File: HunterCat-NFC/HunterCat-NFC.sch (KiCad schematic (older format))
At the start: 60 parts, among them P1 USB_C_Plug_USB2.0, SW1 RESET, U1 ATSAMD21E18A, U2 PN7150B0HN/C11004, U3 MCP73831-3-OT, Y1 27.12Mhz

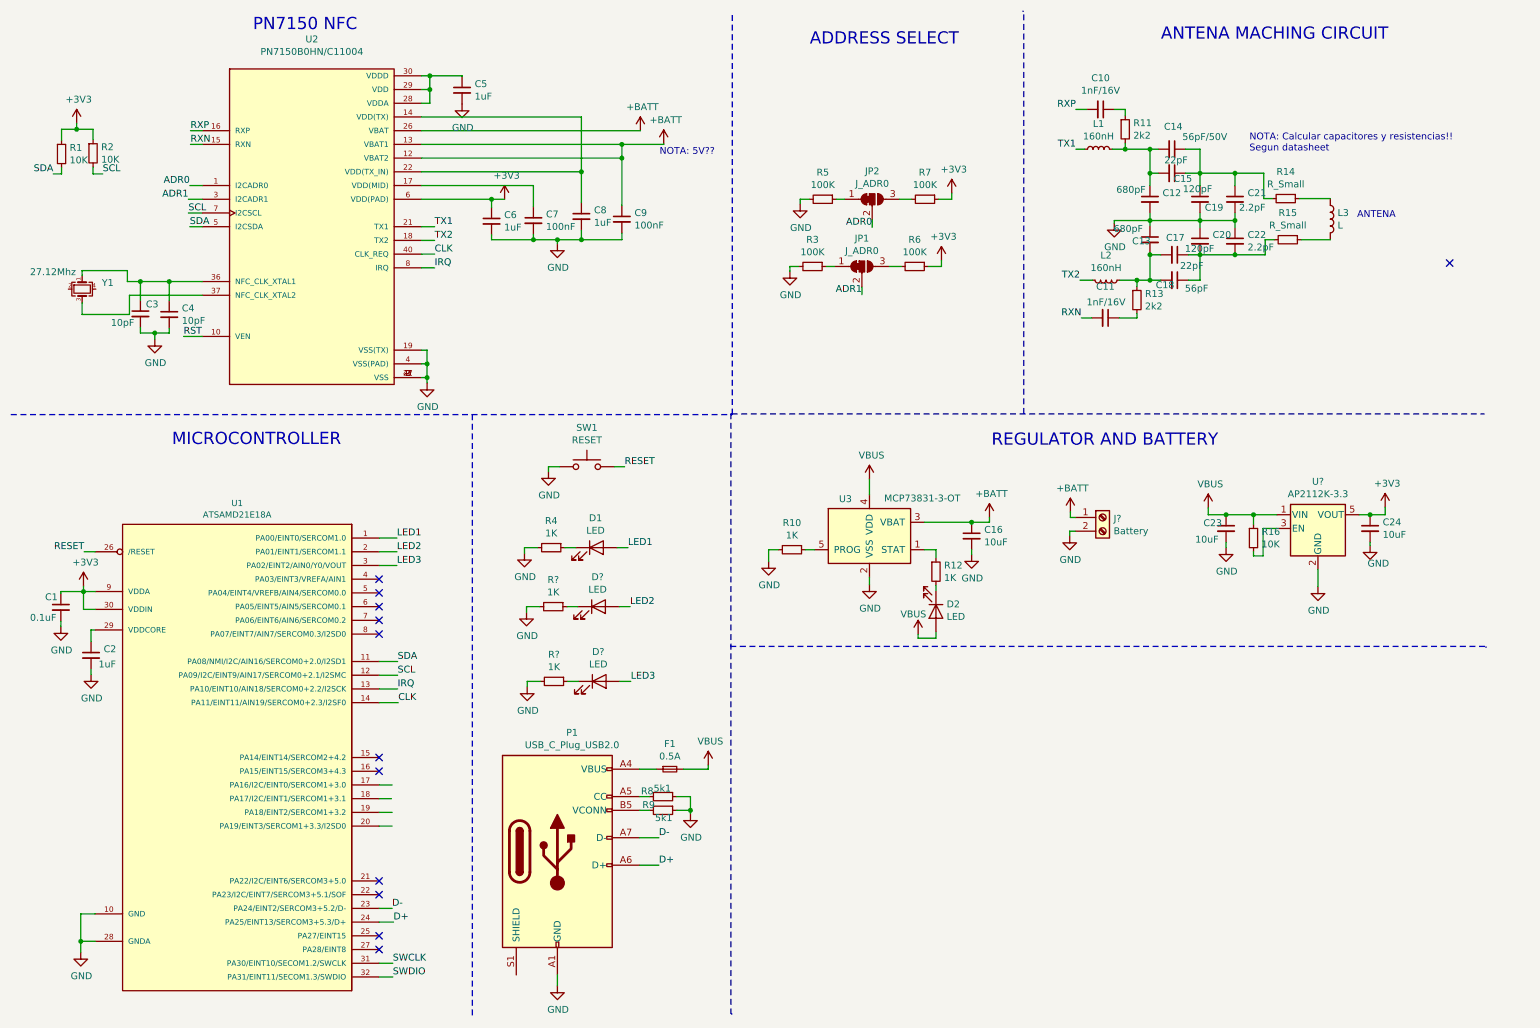
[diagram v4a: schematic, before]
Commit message: add SPI flash and ADC Battery
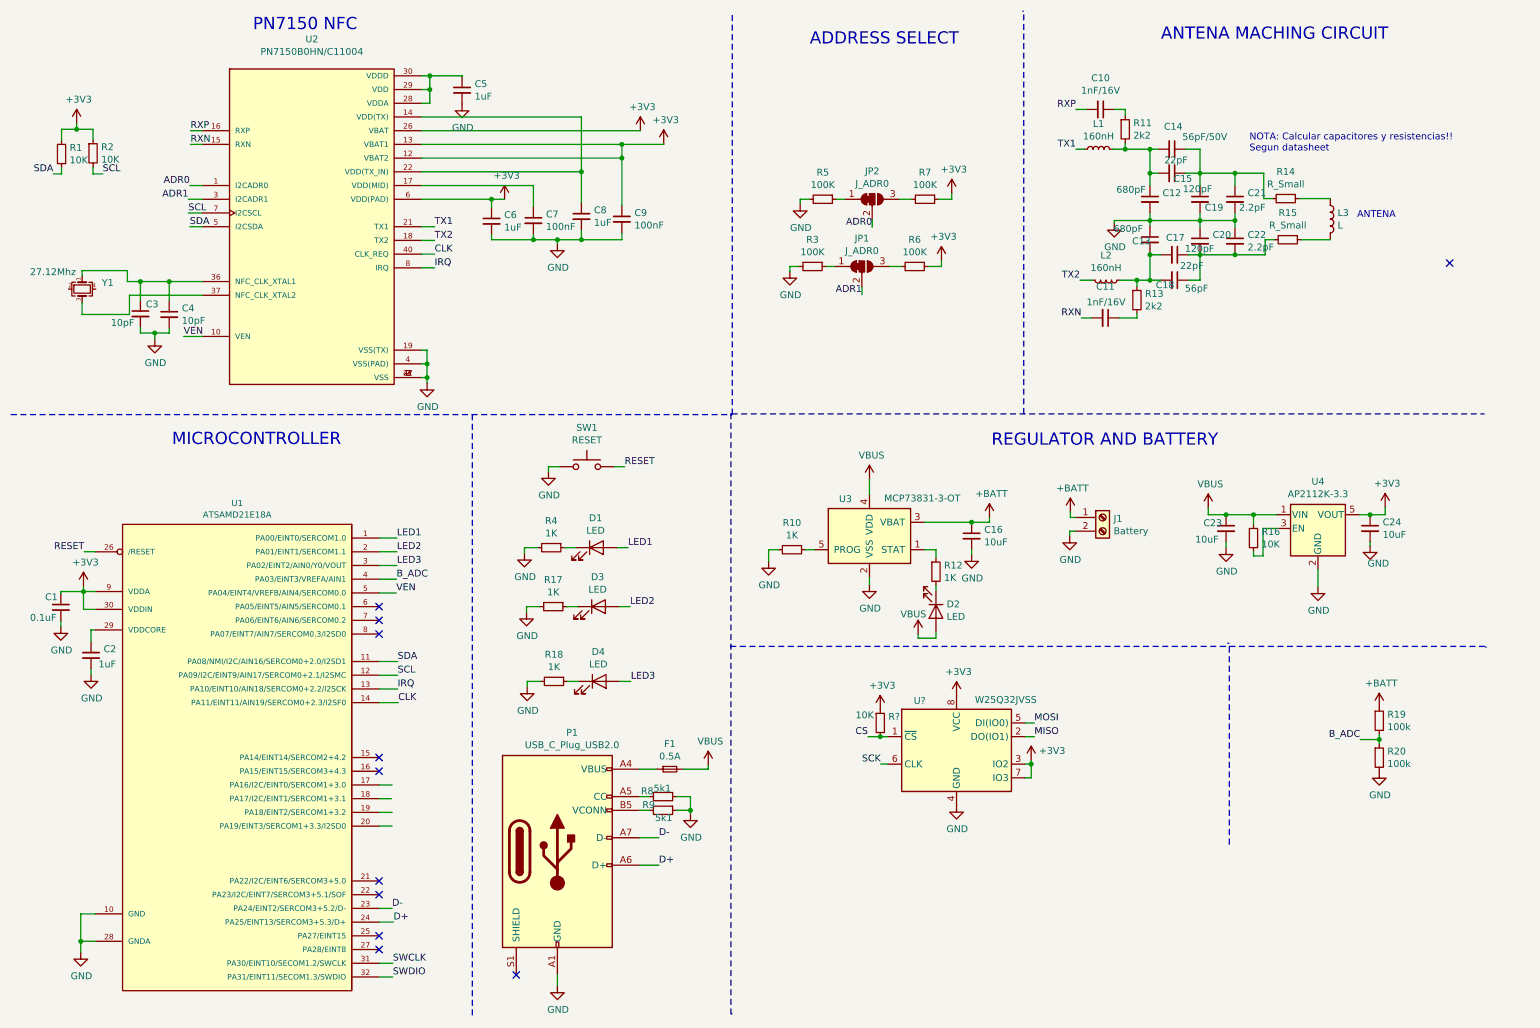
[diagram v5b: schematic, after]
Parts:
- added R19, R20: 100k, symbol Device:R_Small
- added R?: 10K, symbol Device:R_Small
- added U?: W25Q32JVSS, Package_SO:SOIC-8_5.23x5.23mm_P1.27mm, symbol Memory_Flash:W25Q32JVSS
- gave numbers to parts that had none: 6
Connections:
- net RST is gone; now on net VEN: U2.10 (VEN)
- net +3V3: now also C9.1, U2.12 (VBAT2), U2.13 (VBAT1), U2.26 (VBAT), R?.1, U?.3 (IO2), U?.7 (IO3), U?.8 (VCC)
- net +BATT: now also R19.1; no longer C9.1, U2.12 (VBAT2), U2.13 (VBAT1), U2.26 (VBAT)
- net GND: now also R20.2, U?.4 (GND)
- net B_ADC: now reaches U1.4 (PA03/EINT3/VREFA/AIN1)
- net B_ADC: now also R19.2, R20.1
- net VEN: now reaches U1.5 (PA04/EINT4/VREFB/AIN4/SERCOM0.0)
- new net CS: R?.2, U?.1 (~CS)
- new net MISO: U?.2 (DO(IO1))
- new net MOSI: U?.5 (DI(IO0))
- new net SCK: U?.6 (CLK)
- no-connect marks 12 -> 11
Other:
- note removed: "NOTA: 5V??"
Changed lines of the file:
@@
 Connection ~ 4920 1440
-Wire Wire Line
-	3460 1340 5055 1340
 Wire Wire Line
 	3970 1840 4065 1840
@@
 	1860 2840 1725 2840
 Text Label 1725 2840 0    50   ~ 0
-RST
+VEN
 Wire Notes Line
 	465  3410 5725 3410
@@
 	1    0    0    -1
 $EndComp
-$Comp
-L power:+BATT #PWR016
-U 1 1 5E486C1E
-P 5055 1340
-F 0 "#PWR016" H 5055 1190 50  0001 C CNN
-F 1 "+BATT" H 5070 1513 50  0000 C CNN
-F 2 "" H 5055 1340 50  0001 C CNN
-F 3 "" H 5055 1340 50  0001 C CNN
-	1    5055 1340
-	1    0    0    -1
-$EndComp
-$Comp
-L power:+BATT #PWR017
-U 1 1 5E4874CB
-P 5225 1435
-F 0 "#PWR017" H 5225 1285 50  0001 C CNN
-F 1 "+BATT" H 5240 1608 50  0000 C CNN
-F 2 "" H 5225 1435 50  0001 C CNN
-F 3 "" H 5225 1435 50  0001 C CNN
-	1    5225 1435
-	1    0    0    -1
-$EndComp
 Wire Wire Line
 	5225 1440 5225 1435
 Wire Wire Line
 	4920 1440 5225 1440
-Text Notes 5195 1525 0    50   ~ 0
-NOTA: 5V??
 $Comp
 L Device:R_Small R1
@@
 $EndComp
 $Comp
-L Connector:Screw_Terminal_01x02 J?
+L Connector:Screw_Terminal_01x02 J1
 U 1 1 5E75338C
 P 8425 4160
-F 0 "J?" H 8505 4152 50  0000 L CNN
+F 0 "J1" H 8505 4152 50  0000 L CNN
 F 1 "Battery" H 8505 4061 50  0000 L CNN
 F 2 "" H 8425 4160 50  0001 C CNN
@@
 	8185 4260 8185 4295
 $Comp
-L power:GND #PWR?
+L power:GND #PWR0101
 U 1 1 5E76E2B6
 P 8185 4295
-F 0 "#PWR?" H 8185 4045 50  0001 C CNN
+F 0 "#PWR0101" H 8185 4045 50  0001 C CNN
 F 1 "GND" H 8190 4122 50  0000 C CNN
 F 2 "" H 8185 4295 50  0001 C CNN
@@
 $EndComp
 $Comp
-L power:+BATT #PWR?
+L power:+BATT #PWR0102
 U 1 1 5E76EF50
 P 8190 4120
-F 0 "#PWR?" H 8190 3970 50  0001 C CNN
+F 0 "#PWR0102" H 8190 3970 50  0001 C CNN
 F 1 "+BATT" H 8205 4293 50  0000 C CNN
 F 2 "" H 8190 4120 50  0001 C CNN
@@
 $EndComp
 $Comp
-L Device:LED D?
+L Device:LED D3
 U 1 1 5E770C69
 P 4750 4810
-F 0 "D?" H 4743 5026 50  0000 C CNN
+F 0 "D3" H 4743 5026 50  0000 C CNN
 F 1 "LED" H 4743 4935 50  0000 C CNN
 F 2 "" H 4750 4810 50  0001 C CNN
@@
 $EndComp
 $Comp
-L Device:R_Small R?
+L Device:R_Small R17
 U 1 1 5E770C6F
 P 4420 4810
-F 0 "R?" V 4224 4810 50  0000 C CNN
+F 0 "R17" V 4224 4810 50  0000 C CNN
 F 1 "1K" V 4315 4810 50  0000 C CNN
 F 2 "" H 4420 4810 50  0001 C CNN
@@
 	4900 4810 4980 4810
 $Comp
-L power:GND #PWR?
+L power:GND #PWR0103
 U 1 1 5E770C79
 P 4225 4850
-F 0 "#PWR?" H 4225 4600 50  0001 C CNN
+F 0 "#PWR0103" H 4225 4600 50  0001 C CNN
 F 1 "GND" H 4230 4677 50  0000 C CNN
 F 2 "" H 4225 4850 50  0001 C CNN
@@
 LED2
 $Comp
-L Device:LED D?
+L Device:LED D4
 U 1 1 5E793493
 P 4755 5355
-F 0 "D?" H 4748 5571 50  0000 C CNN
+F 0 "D4" H 4748 5571 50  0000 C CNN
 F 1 "LED" H 4748 5480 50  0000 C CNN
 F 2 "" H 4755 5355 50  0001 C CNN
@@
 $EndComp
 $Comp
-L Device:R_Small R?
+L Device:R_Small R18
 U 1 1 5E793499
 P 4425 5355
-F 0 "R?" V 4229 5355 50  0000 C CNN
+F 0 "R18" V 4229 5355 50  0000 C CNN
 F 1 "1K" V 4320 5355 50  0000 C CNN
 F 2 "" H 4425 5355 50  0001 C CNN
@@
 	4905 5355 4985 5355
 $Comp
-L power:GND #PWR?
+L power:GND #PWR0104
 U 1 1 5E7934A3
 P 4230 5395
-F 0 "#PWR?" H 4230 5145 50  0001 C CNN
+F 0 "#PWR0104" H 4230 5145 50  0001 C CNN
 F 1 "GND" H 4235 5222 50  0000 C CNN
 F 2 "" H 4230 5395 50  0001 C CNN
@@
 Text Label 4985 5355 0    50   ~ 0
 LED3
-NoConn ~ 3150 4610
-NoConn ~ 3150 4710
 NoConn ~ 3150 4810
 NoConn ~ 3150 4910
@@
 	7850 470  7840 470
 $Comp
-L Regulator_Linear:AP2112K-3.3 U?
+L Regulator_Linear:AP2112K-3.3 U4
 U 1 1 5E451F7B
 P 9995 4240
-F 0 "U?" H 9995 4582 50  0000 C CNN
+F 0 "U4" H 9995 4582 50  0000 C CNN
 F 1 "AP2112K-3.3" H 9995 4491 50  0000 C CNN
 F 2 "Package_TO_SOT_SMD:SOT-23-5" H 9995 4565 50  0001 C CNN
@@
 Wire Wire Line
 	9525 4440 9525 4410
+Wire Wire Line
+	3460 1340 5055 1340
+$Comp
+L power:+3V3 #PWR0105
+U 1 1 5E67D6C7
+P 5225 1435
+F 0 "#PWR0105" H 5225 1285 50  0001 C CNN
+F 1 "+3V3" H 5240 1608 50  0000 C CNN
+F 2 "" H 5225 1435 50  0001 C CNN
+F 3 "" H 5225 1435 50  0001 C CNN
+	1    5225 1435
+	1    0    0    -1
+$EndComp
+$Comp
+L power:+3V3 #PWR0106
+U 1 1 5E67E264
+P 5055 1340
+F 0 "#PWR0106" H 5055 1190 50  0001 C CNN
+F 1 "+3V3" H 5070 1513 50  0000 C CNN
+F 2 "" H 5055 1340 50  0001 C CNN
+F 3 "" H 5055 1340 50  0001 C CNN
+	1    5055 1340
+	1    0    0    -1
+$EndComp
+Wire Wire Line
+	3150 4710 3275 4710
+Text Label 3275 4710 0    50   ~ 0
+VEN
+Wire Wire Line
+	3150 4610 3277 4610
+Text Label 3277 4610 0    50   ~ 0
+B_ADC
+$Comp
+L Device:R_Small R19
+U 1 1 5E6BD0A2
+P 10442 5642
+F 0 "R19" H 10501 5688 50  0000 L CNN
+F 1 "100k" H 10501 5597 50  0000 L CNN
+F 2 "" H 10442 5642 50  0001 C CNN
+F 3 "~" H 10442 5642 50  0001 C CNN
+	1    10442 5642
+	1    0    0    -1
+$EndComp
+$Comp
+L Device:R_Small R20
+U 1 1 5E6BDB90
+P 10442 5911
+F 0 "R20" H 10501 5957 50  0000 L CNN
+F 1 "100k" H 10501 5866 50  0000 L CNN
+F 2 "" H 10442 5911 50  0001 C CNN
+F 3 "~" H 10442 5911 50  0001 C CNN
+	1    10442 5911
+	1    0    0    -1
+$EndComp
+Wire Wire Line
+	10442 5742 10442 5779
+Wire Wire Line
+	10442 5779 10303 5779
+Connection ~ 10442 5779
+Wire Wire Line
+	10442 5779 10442 5811
+Text Label 10303 5779 2    50   ~ 0
+B_ADC
+$Comp
+L power:+BATT #PWR0107
+U 1 1 5E6DD27D
+P 10442 5542
+F 0 "#PWR0107" H 10442 5392 50  0001 C CNN
+F 1 "+BATT" H 10457 5715 50  0000 C CNN
+F 2 "" H 10442 5542 50  0001 C CNN
+F 3 "" H 10442 5542 50  0001 C CNN
+	1    10442 5542
+	1    0    0    -1
+$EndComp
+$Comp
+L power:GND #PWR0108
+U 1 1 5E6DE2AB
+P 10442 6011
+F 0 "#PWR0108" H 10442 5761 50  0001 C CNN
+F 1 "GND" H 10447 5838 50  0000 C CNN
+F 2 "" H 10442 6011 50  0001 C CNN
+F 3 "" H 10442 6011 50  0001 C CNN
+	1    10442 6011
+	1    0    0    -1
+$EndComp
+NoConn ~ 4150 7495
+Wire Notes Line
+	9349 6545 9349 5077
+Wire Notes Line
+	9349 5077 9335 5077
+$Comp
+L Memory_Flash:W25Q32JVSS U?
+U 1 1 5E73BDBA
+P 7360 5858
+F 0 "U?" H 7091 6220 50  0000 C CNN
+F 1 "W25Q32JVSS" H 7719 6227 50  0000 C CNN
+F 2 "Package_SO:SOIC-8_5.23x5.23mm_P1.27mm" H 7360 5858 50  0001 C CNN
+F 3 "http://www.winbond.com/resource-files/w25q32jv%20revg%2003272018%20plus.pdf" H 7360 5858 50  0001 C CNN
+	1    7360 5858
+	1    0    0    -1
+$EndComp
+$Comp
+L power:GND #PWR?
+U 1 1 5E73D4E9
+P 7360 6258
+F 0 "#PWR?" H 7360 6008 50  0001 C CNN
+F 1 "GND" H 7365 6085 50  0000 C CNN
+F 2 "" H 7360 6258 50  0001 C CNN
+F 3 "" H 7360 6258 50  0001 C CNN
+	1    7360 6258
+	1    0    0    -1
+$EndComp
+$Comp
+L power:+3V3 #PWR?
+U 1 1 5E73E614
+P 7360 5458
+F 0 "#PWR?" H 7360 5308 50  0001 C CNN
+F 1 "+3V3" H 7375 5631 50  0000 C CNN
+F 2 "" H 7360 5458 50  0001 C CNN
+F 3 "" H 7360 5458 50  0001 C CNN
+	1    7360 5458
+	1    0    0    -1
+$EndComp
+Wire Wire Line
+	7905 6058 7905 5958
+Wire Wire Line
+	7905 5958 7904 5958
+Wire Wire Line
+	7860 6058 7905 6058
+Wire Wire Line
+	7904 5958 7904 5928
+Connection ~ 7904 5958
+Wire Wire Line
+	7904 5958 7860 5958
+$Comp
+L power:+3V3 #PWR?
+U 1 1 5E76F067
+P 7904 5928
+F 0 "#PWR?" H 7904 5778 50  0001 C CNN
+F 1 "+3V3" H 8057 5995 50  0000 C CNN
+F 2 "" H 7904 5928 50  0001 C CNN
+F 3 "" H 7904 5928 50  0001 C CNN
+	1    7904 5928
+	1    0    0    -1
+$EndComp
+Wire Wire Line
+	7860 5658 7927 5658
+Wire Wire Line
+	7860 5758 7928 5758
+Wire Wire Line
+	6860 5758 6804 5758
+Wire Wire Line
+	6860 5958 6807 5958
+$Comp
+L Device:R_Small R?
+U 1 1 5E7C0D45
+P 6804 5658
+F 0 "R?" H 6863 5704 50  0000 L CNN
+F 1 "10K" H 6624 5715 50  0000 L CNN
+F 2 "" H 6804 5658 50  0001 C CNN
+F 3 "~" H 6804 5658 50  0001 C CNN
+	1    6804 5658
+	1    0    0    -1
+$EndComp
+$Comp
+L power:+3V3 #PWR?
+U 1 1 5E7C254D
+P 6804 5558
+F 0 "#PWR?" H 6804 5408 50  0001 C CNN
+F 1 "+3V3" H 6819 5731 50  0000 C CNN
+F 2 "" H 6804 5558 50  0001 C CNN
+F 3 "" H 6804 5558 50  0001 C CNN
+	1    6804 5558
+	1    0    0    -1
+$EndComp
+Text Label 6714 5758 2    50   ~ 0
+CS
+Wire Wire Line
+	6804 5758 6714 5758
+Connection ~ 6804 5758
+Text Label 6807 5958 2    50   ~ 0
+SCK
+Text Label 7928 5758 0    50   ~ 0
+MISO
+Text Label 7927 5658 0    50   ~ 0
+MOSI
 $EndSCHEMATC

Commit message: add SPI pins
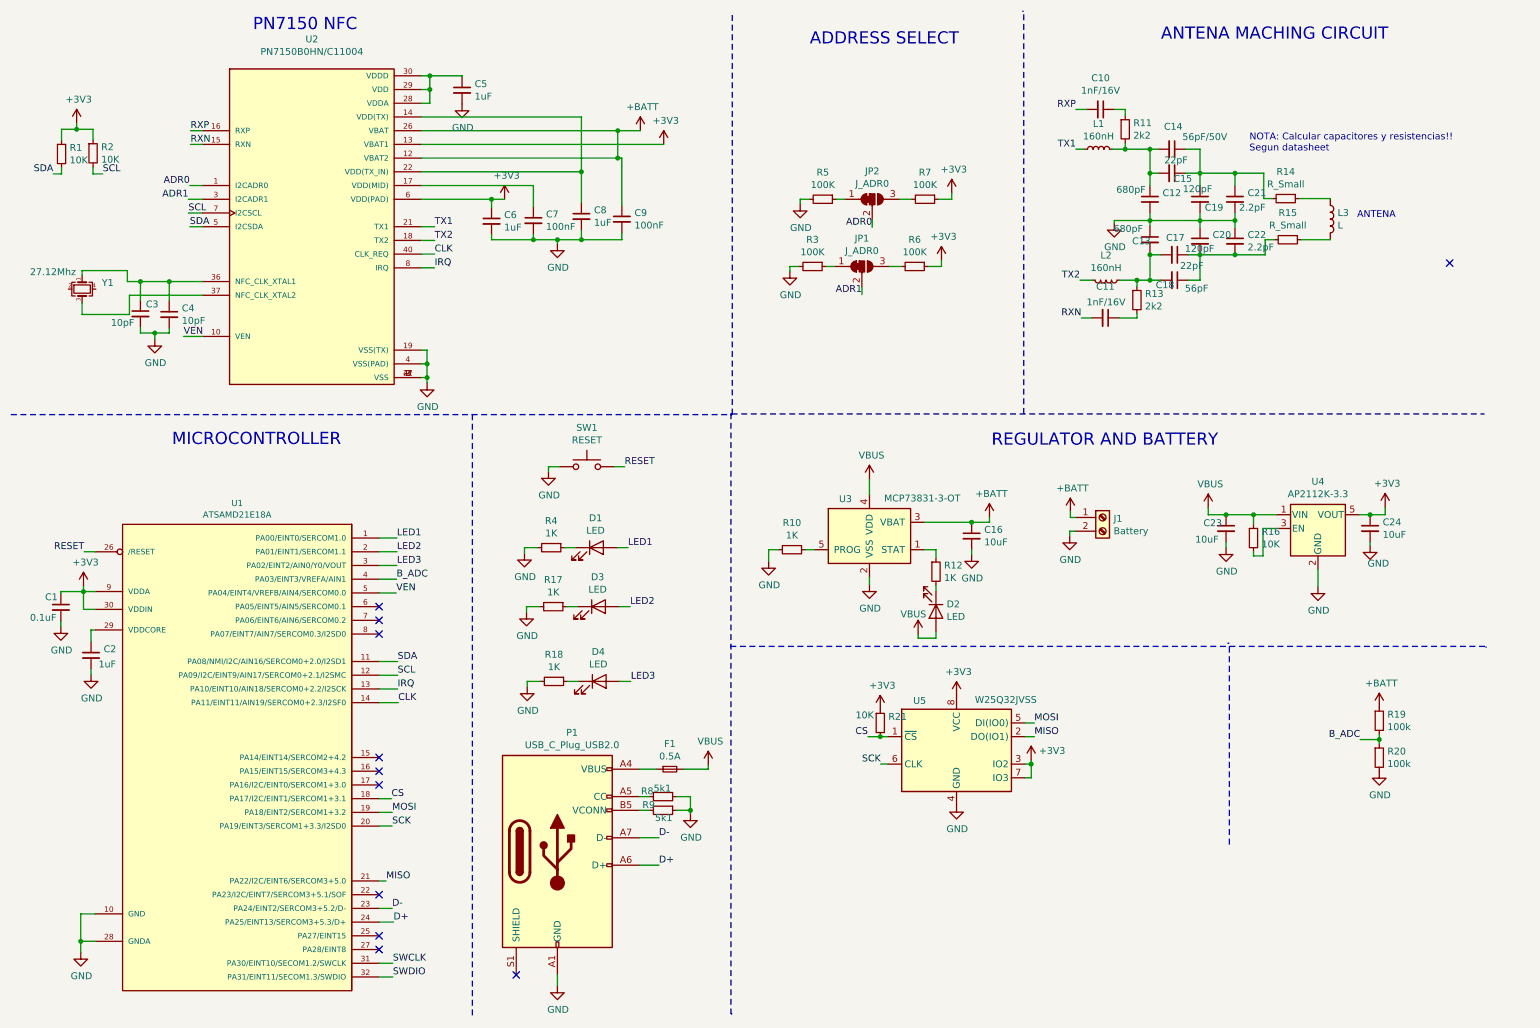
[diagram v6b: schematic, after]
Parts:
- gave numbers to parts that had none: 2
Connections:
- net +3V3: no longer C9.1, U2.12 (VBAT2), U2.26 (VBAT)
- net +BATT: now also C9.1, U2.12 (VBAT2), U2.26 (VBAT)
- net CS: now also U1.18 (PA17/I2C/EINT1/SERCOM1+3.1)
- net MISO: now also U1.21 (PA22/I2C/EINT6/SERCOM3+5.0)
- net MOSI: now also U1.19 (PA18/EINT2/SERCOM1+3.2)
- net SCK: now also U1.20 (PA19/EINT3/SERCOM1+3.3/I2SD0)
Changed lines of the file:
@@
 $EndComp
-Wire Wire Line
-	4920 1440 4920 1540
-Wire Wire Line
-	3460 1540 4920 1540
-Connection ~ 4920 1540
 Wire Wire Line
 	4920 1540 4920 1885
@@
 	1    0    0    -1
 $EndComp
-Wire Wire Line
-	3460 1440 4920 1440
-Connection ~ 4920 1440
 Wire Wire Line
 	3970 1840 4065 1840
@@
 	3150 6210 3240 6210
 Wire Wire Line
-	3150 6110 3245 6110
-Wire Wire Line
 	3150 6410 3245 6410
 Wire Wire Line
@@
 	1    0    0    -1
 $EndComp
-Wire Wire Line
-	5225 1440 5225 1435
-Wire Wire Line
-	4920 1440 5225 1440
 $Comp
 L Device:R_Small R1
@@
 NoConn ~ 3150 7210
 NoConn ~ 3150 6910
-NoConn ~ 3150 6810
 NoConn ~ 10955 2305
 Text Notes 7615 3650 0    89   ~ 0
@@
 	9525 4440 9525 4410
 Wire Wire Line
-	3460 1340 5055 1340
-$Comp
-L power:+3V3 #PWR0105
-U 1 1 5E67D6C7
-P 5225 1435
-F 0 "#PWR0105" H 5225 1285 50  0001 C CNN
-F 1 "+3V3" H 5240 1608 50  0000 C CNN
-F 2 "" H 5225 1435 50  0001 C CNN
-F 3 "" H 5225 1435 50  0001 C CNN
-	1    5225 1435
-	1    0    0    -1
-$EndComp
-$Comp
-L power:+3V3 #PWR0106
-U 1 1 5E67E264
-P 5055 1340
-F 0 "#PWR0106" H 5055 1190 50  0001 C CNN
-F 1 "+3V3" H 5070 1513 50  0000 C CNN
-F 2 "" H 5055 1340 50  0001 C CNN
-F 3 "" H 5055 1340 50  0001 C CNN
-	1    5055 1340
-	1    0    0    -1
-$EndComp
+	3460 1340 4890 1340
 Wire Wire Line
 	3150 4710 3275 4710
@@
 	9349 5077 9335 5077
 $Comp
-L Memory_Flash:W25Q32JVSS U?
+L Memory_Flash:W25Q32JVSS U5
 U 1 1 5E73BDBA
 P 7360 5858
-F 0 "U?" H 7091 6220 50  0000 C CNN
+F 0 "U5" H 7091 6220 50  0000 C CNN
 F 1 "W25Q32JVSS" H 7719 6227 50  0000 C CNN
 F 2 "Package_SO:SOIC-8_5.23x5.23mm_P1.27mm" H 7360 5858 50  0001 C CNN
@@
 $EndComp
 $Comp
-L power:GND #PWR?
+L power:GND #PWR036
 U 1 1 5E73D4E9
 P 7360 6258
-F 0 "#PWR?" H 7360 6008 50  0001 C CNN
+F 0 "#PWR036" H 7360 6008 50  0001 C CNN
 F 1 "GND" H 7365 6085 50  0000 C CNN
 F 2 "" H 7360 6258 50  0001 C CNN
@@
 $EndComp
 $Comp
-L power:+3V3 #PWR?
+L power:+3V3 #PWR035
 U 1 1 5E73E614
 P 7360 5458
-F 0 "#PWR?" H 7360 5308 50  0001 C CNN
+F 0 "#PWR035" H 7360 5308 50  0001 C CNN
 F 1 "+3V3" H 7375 5631 50  0000 C CNN
 F 2 "" H 7360 5458 50  0001 C CNN
@@
 	7904 5958 7860 5958
 $Comp
-L power:+3V3 #PWR?
+L power:+3V3 #PWR037
 U 1 1 5E76F067
 P 7904 5928
-F 0 "#PWR?" H 7904 5778 50  0001 C CNN
+F 0 "#PWR037" H 7904 5778 50  0001 C CNN
 F 1 "+3V3" H 8057 5995 50  0000 C CNN
 F 2 "" H 7904 5928 50  0001 C CNN
@@
 	6860 5958 6807 5958
 $Comp
-L Device:R_Small R?
+L Device:R_Small R21
 U 1 1 5E7C0D45
 P 6804 5658
-F 0 "R?" H 6863 5704 50  0000 L CNN
+F 0 "R21" H 6863 5704 50  0000 L CNN
 F 1 "10K" H 6624 5715 50  0000 L CNN
 F 2 "" H 6804 5658 50  0001 C CNN
@@
 $EndComp
 $Comp
-L power:+3V3 #PWR?
+L power:+3V3 #PWR034
 U 1 1 5E7C254D
 P 6804 5558
-F 0 "#PWR?" H 6804 5408 50  0001 C CNN
+F 0 "#PWR034" H 6804 5408 50  0001 C CNN
 F 1 "+3V3" H 6819 5731 50  0000 C CNN
 F 2 "" H 6804 5558 50  0001 C CNN
@@
 Text Label 7927 5658 0    50   ~ 0
 MOSI
+Wire Wire Line
+	3460 1440 5225 1440
+$Comp
+L power:+BATT #PWR016
+U 1 1 5E8068AB
+P 5055 1340
+F 0 "#PWR016" H 5055 1190 50  0001 C CNN
+F 1 "+BATT" H 5070 1513 50  0000 C CNN
+F 2 "" H 5055 1340 50  0001 C CNN
+F 3 "" H 5055 1340 50  0001 C CNN
+	1    5055 1340
+	1    0    0    -1
+$EndComp
+Wire Wire Line
+	4890 1540 4890 1340
+Wire Wire Line
+	3460 1540 4890 1540
+Connection ~ 4890 1540
+Wire Wire Line
+	4890 1540 4920 1540
+Connection ~ 4890 1340
+Wire Wire Line
+	4890 1340 5055 1340
+$Comp
+L power:+3V3 #PWR017
+U 1 1 5E819D40
+P 5225 1440
+F 0 "#PWR017" H 5225 1290 50  0001 C CNN
+F 1 "+3V3" H 5240 1613 50  0000 C CNN
+F 2 "" H 5225 1440 50  0001 C CNN
+F 3 "" H 5225 1440 50  0001 C CNN
+	1    5225 1440
+	1    0    0    -1
+$EndComp
+Text Label 3240 6210 0    50   ~ 0
+CS
+Text Label 3245 6310 0    50   ~ 0
+MOSI
+Text Label 3245 6410 0    50   ~ 0
+SCK
+Wire Wire Line
+	3150 6810 3201 6810
+Text Label 3201 6810 0    50   ~ 0
+MISO
+NoConn ~ 3150 6110
 $EndSCHEMATC
